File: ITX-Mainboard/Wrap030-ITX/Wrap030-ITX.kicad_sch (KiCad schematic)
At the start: 0 parts

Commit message: Schematic substantial completion
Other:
- added sheet ISA-IDE (ISA-IDE.kicad_sch)
- added sheet Keyboard (keyboard.kicad_sch)
- added sheet Power-Supply (power.kicad_sch)
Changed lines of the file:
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@@
     (company "techav")
+  )
+  (sheet (at 25.4 127) (size 25.4 3.81) (fields_autoplaced)
+    (stroke (width 0.1524) (type solid))
+    (fill (color 0 0 0 0.0000))
+    (property "Sheetname" "Keyboard" (at 25.4 126.2884 0)
+      (effects (font (size 1.27 1.27)) (justify left bottom))
+    )
+    (property "Sheetfile" "keyboard.kicad_sch" (at 25.4 131.3946 0)
+      (effects (font (size 1.27 1.27)) (justify left top))
+    )
+    (instances
+      (project "Wrap030-ITX"
+        (path "/911cb688-7d4c-4194-bbd3-2b645bd8d53c" (page "11"))
+      )
+    )
   )
   (sheet (at 25.4 88.9) (size 25.4 3.81) (fields_autoplaced)
@@
       (project "Wrap030-ITX"
         (path "/911cb688-7d4c-4194-bbd3-2b645bd8d53c" (page "7"))
+      )
+    )
+  )
+  (sheet (at 25.4 101.6) (size 25.4 3.81) (fields_autoplaced)
+    (stroke (width 0.1524) (type solid))
+    (fill (color 0 0 0 0.0000))
+    (property "Sheetname" "ISA-IDE" (at 25.4 100.8884 0)
+      (effects (font (size 1.27 1.27)) (justify left bottom))
+    )
+    (property "Sheetfile" "ISA-IDE.kicad_sch" (at 25.4 105.9946 0)
+      (effects (font (size 1.27 1.27)) (justify left top))
+    )
+    (instances
+      (project "Wrap030-ITX"
+        (path "/911cb688-7d4c-4194-bbd3-2b645bd8d53c" (page "8"))
       )
     )
@@
       )
     )
+  )
+  (sheet (at 25.4 114.3) (size 25.4 3.81) (fields_autoplaced)
+    (stroke (width 0.1524) (type solid))
+    (fill (color 0 0 0 0.0000))
+    (property "Sheetname" "Power-Supply" (at 25.4 113.5884 0)
+      (effects (font (size 1.27 1.27)) (justify left bottom))
+    )
+    (property "Sheetfile" "power.kicad_sch" (at 25.4 118.6946 0)
+      (effects (font (size 1.27 1.27)) (justify left top))
+    )
+    (instances
+      (project "Wrap030-ITX"
+        (path "/911cb688-7d4c-4194-bbd3-2b645bd8d53c" (page "10"))
+      )
+    )

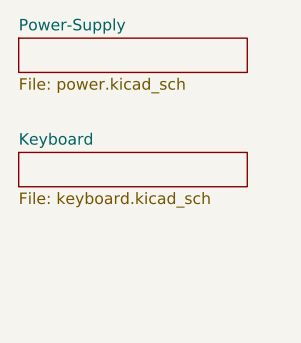
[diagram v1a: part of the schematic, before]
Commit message: Add interrupt controller to schematic
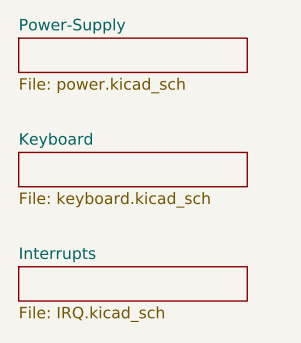
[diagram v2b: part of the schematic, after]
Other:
- added sheet Interrupts (IRQ.kicad_sch)
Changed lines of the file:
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@@
+    )
+  )
+  (sheet (at 25.4 139.7) (size 25.4 3.81) (fields_autoplaced)
+    (stroke (width 0.1524) (type solid))
+    (fill (color 0 0 0 0.0000))
+    (property "Sheetname" "Interrupts" (at 25.4 138.9884 0)
+      (effects (font (size 1.27 1.27)) (justify left bottom))
+    )
+    (property "Sheetfile" "IRQ.kicad_sch" (at 25.4 144.0946 0)
+      (effects (font (size 1.27 1.27)) (justify left top))
+    )
+    (instances
+      (project "Wrap030-ITX"
+        (path "/911cb688-7d4c-4194-bbd3-2b645bd8d53c" (page "12"))
+      )
     )
   )

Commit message: Completing PCB Routing
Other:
- title: Wrap030 ITX -> Wrap030-ATX Mainboard
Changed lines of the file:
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@@
   (paper "USLetter")
   (title_block
-    (title "Wrap030 ITX")
-    (date "2023-03-15")
-    (rev "0")
+    (title "Wrap030-ATX Mainboard")
+    (date "2023-03-26")
+    (rev "1")
     (company "techav")
   )
